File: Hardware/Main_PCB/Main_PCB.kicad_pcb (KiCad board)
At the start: 2 copper layers, 80 x 35 mm, 86 parts, among them J201 Sonar, J601 Conn_01x08_Pin, J602 Conn_01x03_Pin, J603 Servo con, P301 USB_C_Plug_USB2.0, SW301 TL3342F160QG_TR, SW302 TL3342F160QG_TR, U201 TUSS4470TRTJT, U301 RP2040, U302 W25Q128JVS, U401 TPS62170DSG, U402 TPS61175PWPR, U403 BD50FD0WFP2-E2, U501 ICM-42688-P, U601 NRF24L01, U602 SN74LV1T34DBV, Y301 12Mhz

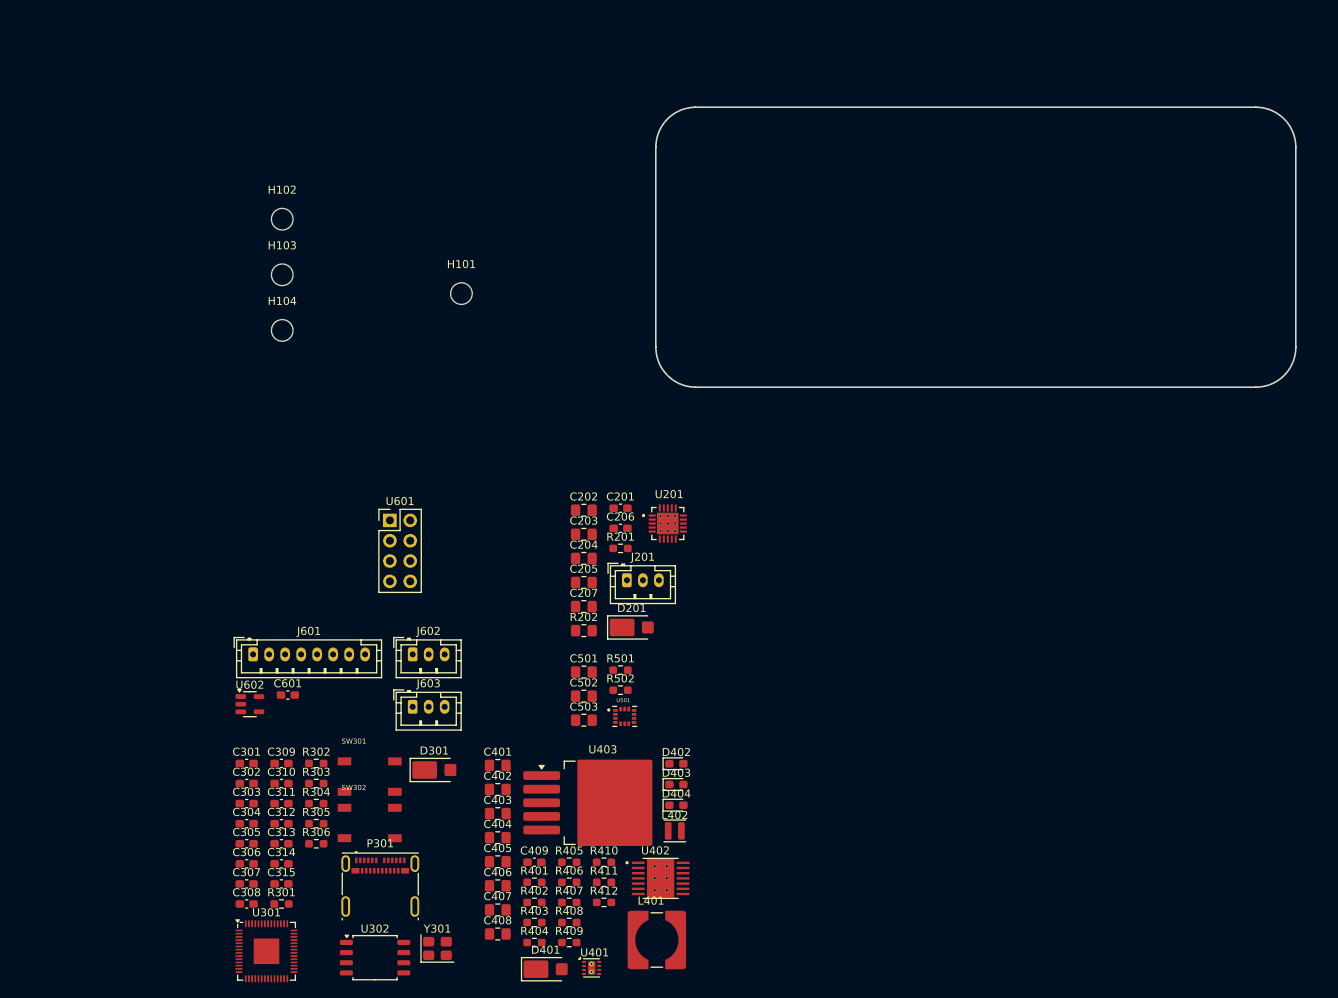
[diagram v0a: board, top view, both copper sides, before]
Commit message: Some footprint positioning
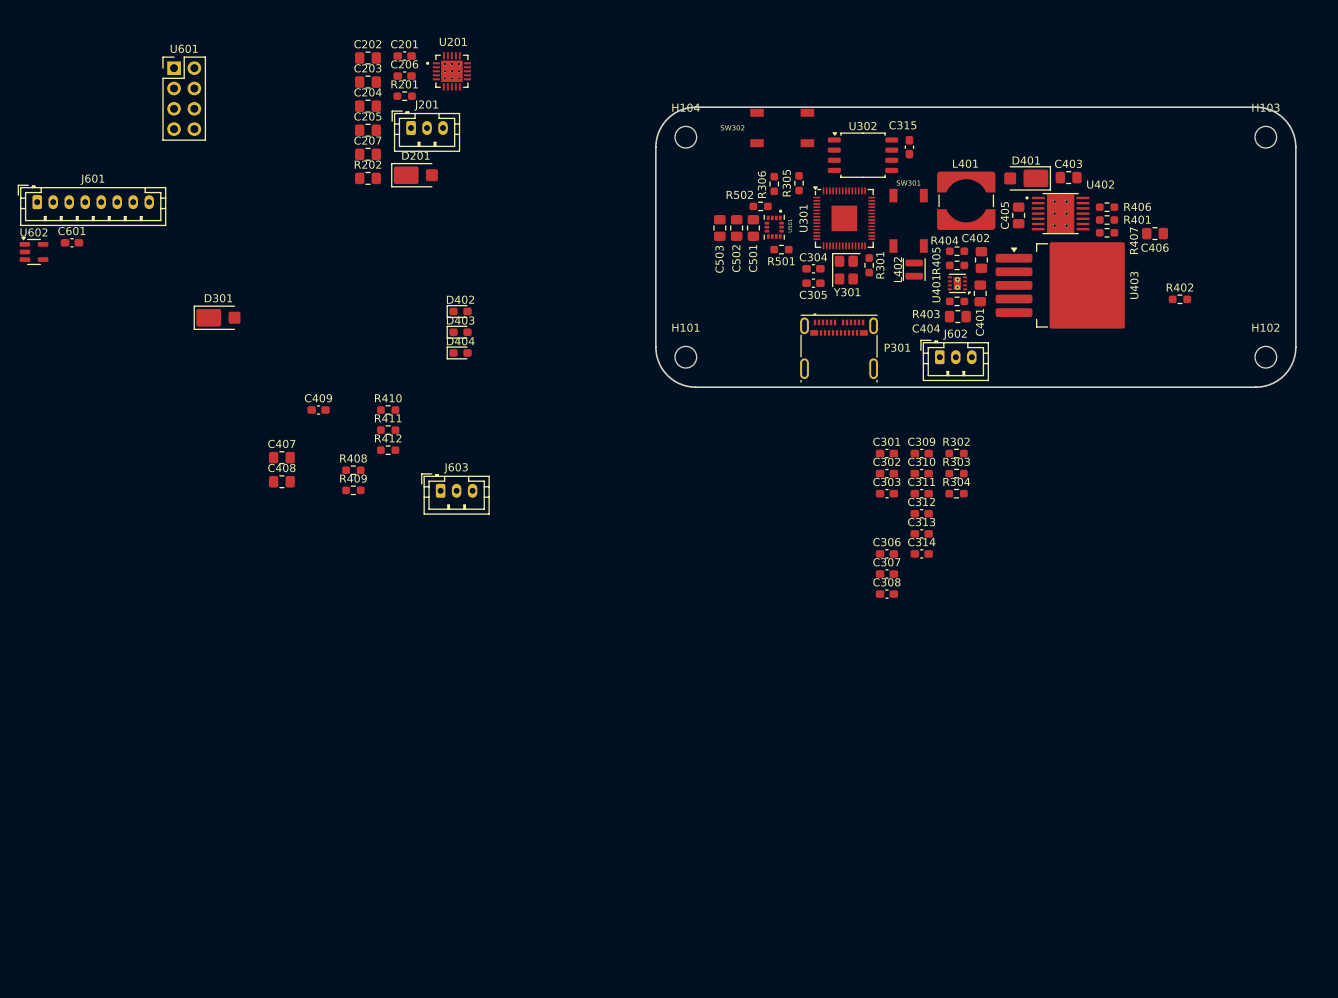
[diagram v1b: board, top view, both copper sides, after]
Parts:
- moved H102 124.2 mm to (191.5, 96.2)
- moved H103 124.1 mm to (191.5, 68.7)
- moved C315 121.0 mm to (146.9, 69.9), turned to -90 degrees
- moved U302 117.4 mm to (141.1, 70.9)
- moved U301 116.7 mm to (138.8, 78.8)
- moved C406 115.7 mm to (177.6, 80.7)
- moved D401 115.7 mm to (161.5, 73.8), turned to 180 degrees
- moved R402 110.4 mm to (180.7, 88.9)
- moved R401 109.4 mm to (171.6, 79.0), turned to 180 degrees
- moved R301 108.5 mm to (141.9, 84.7), turned to -90 degrees
- moved R406 107.9 mm to (171.6, 77.4)
- moved R407 107.4 mm to (171.6, 80.6)
- moved C403 106.8 mm to (166.8, 73.7)
- moved C405 103.8 mm to (160.6, 78.4), turned to 90 degrees
- moved R404 101.3 mm to (152.8, 82.9)
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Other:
- copper layers 2 -> 4

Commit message: Placement almost complete on MainPCB
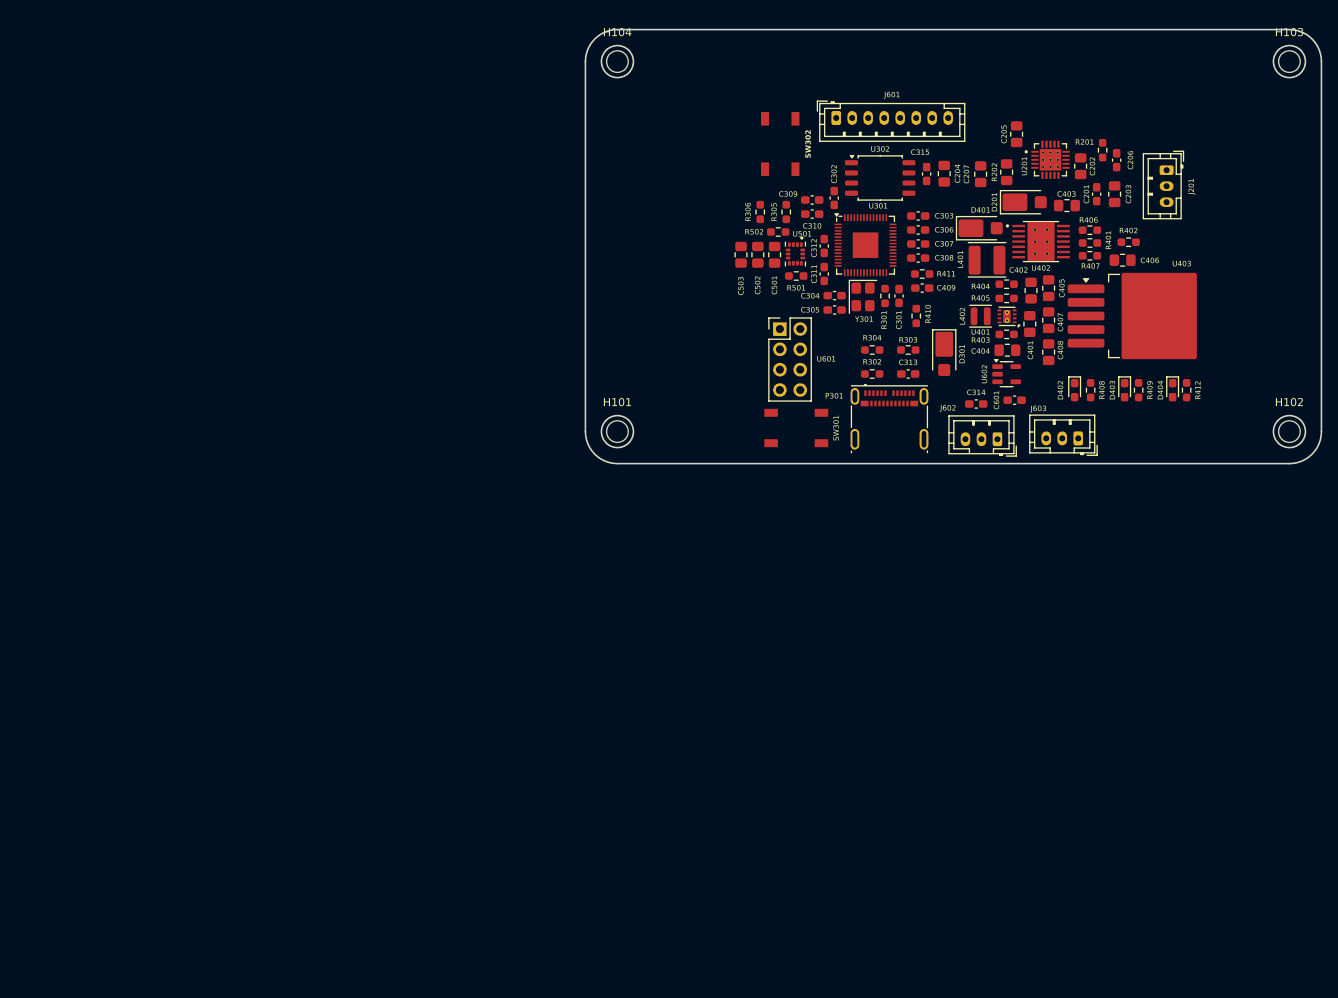
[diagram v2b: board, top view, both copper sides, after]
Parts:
- L401: footprint MainPCB:IND_SRR6038-100Y -> MainPCB:L_33uH
- moved U602 122.5 mm to (159.1, 98.3)
- moved C601 119.5 mm to (160.1, 101.5), turned to 180 degrees
- moved J601 100.4 mm to (137.8, 66.2)
- moved R412 100.1 mm to (181.6, 100.3), turned to -90 degrees
- moved R409 99.0 mm to (175.6, 100.3), turned to -90 degrees
- moved C407 97.4 mm to (164.3, 91.5), turned to -90 degrees
- moved C408 97.2 mm to (164.3, 95.5), turned to -90 degrees
- moved J201 94.6 mm to (179.1, 72.8), turned to -90 degrees
- moved C203 94.4 mm to (172.6, 75.8), turned to 90 degrees
- moved R408 92.7 mm to (169.6, 100.3), turned to -90 degrees
- moved D301 90.8 mm to (151.2, 95.8), turned to -90 degrees
- moved C202 90.1 mm to (168.3, 72.3), turned to 90 degrees
- moved C206 89.6 mm to (172.8, 71.5), turned to -90 degrees
- moved D404 89.1 mm to (179.8, 100.3), turned to -90 degrees
- moved C201 88.2 mm to (170.3, 75.8), turned to 90 degrees
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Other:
- board size 80 x 35 mm -> 92 x 54.2 mm

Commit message: Probably a final version of the MAIN PCB component placement
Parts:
- P301: footprint Connector_USB:USB_C_Receptacle_Molex_105450-0101 -> MainPCB:CUI_UJC-HP-3-SMT-TR
- U601: footprint Connector_PinHeader_2.54mm:PinHeader_2x04_P2.54mm_Vertical -> Connector_PinSocket_2.54mm:PinSocket_2x04_P2.54mm_Vertical
- moved H104 27.5 mm to (137.4, 64.5)
- moved H101 27.0 mm to (137.4, 105.5)
- moved R502 15.3 mm to (145.7, 78.7)
- moved SW301 14.8 mm to (147.6, 105.0)
- moved D402 14.7 mm to (182.2, 98.3)
- moved D403 14.7 mm to (188.4, 98.3)
- moved D404 14.7 mm to (194.4, 98.3)
- moved R408 14.7 mm to (184.2, 98.3)
- moved R409 14.7 mm to (190.2, 98.3)
- moved R412 14.7 mm to (196.2, 98.3)
- moved U501 14.7 mm to (147.2, 81.6)
- moved U403 14.6 mm to (191.2, 90.2)
- moved P301 14.6 mm to (159.0, 102.5)
- moved R305 14.6 mm to (146.0, 76.2)
- moved R306 14.6 mm to (142.7, 76.2)
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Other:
- board outline removed

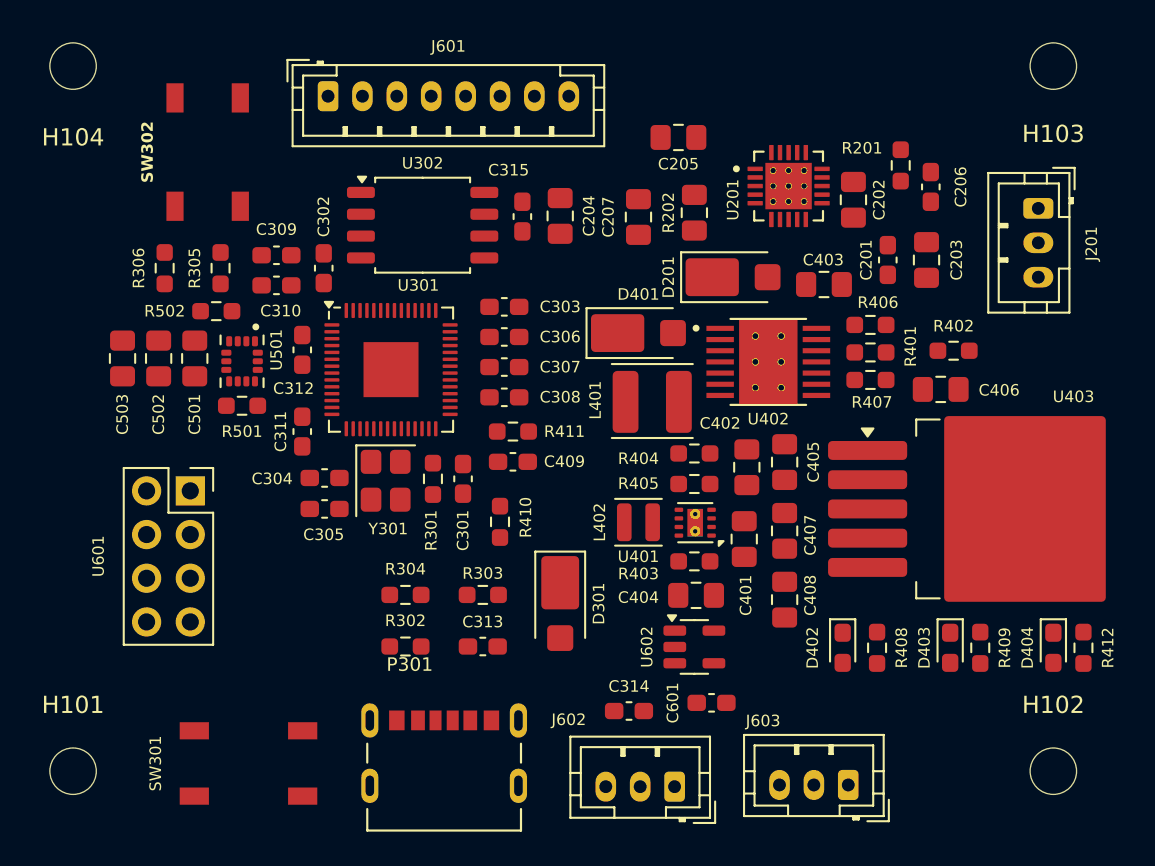
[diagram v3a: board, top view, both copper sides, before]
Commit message: Made the power supply planes and traces
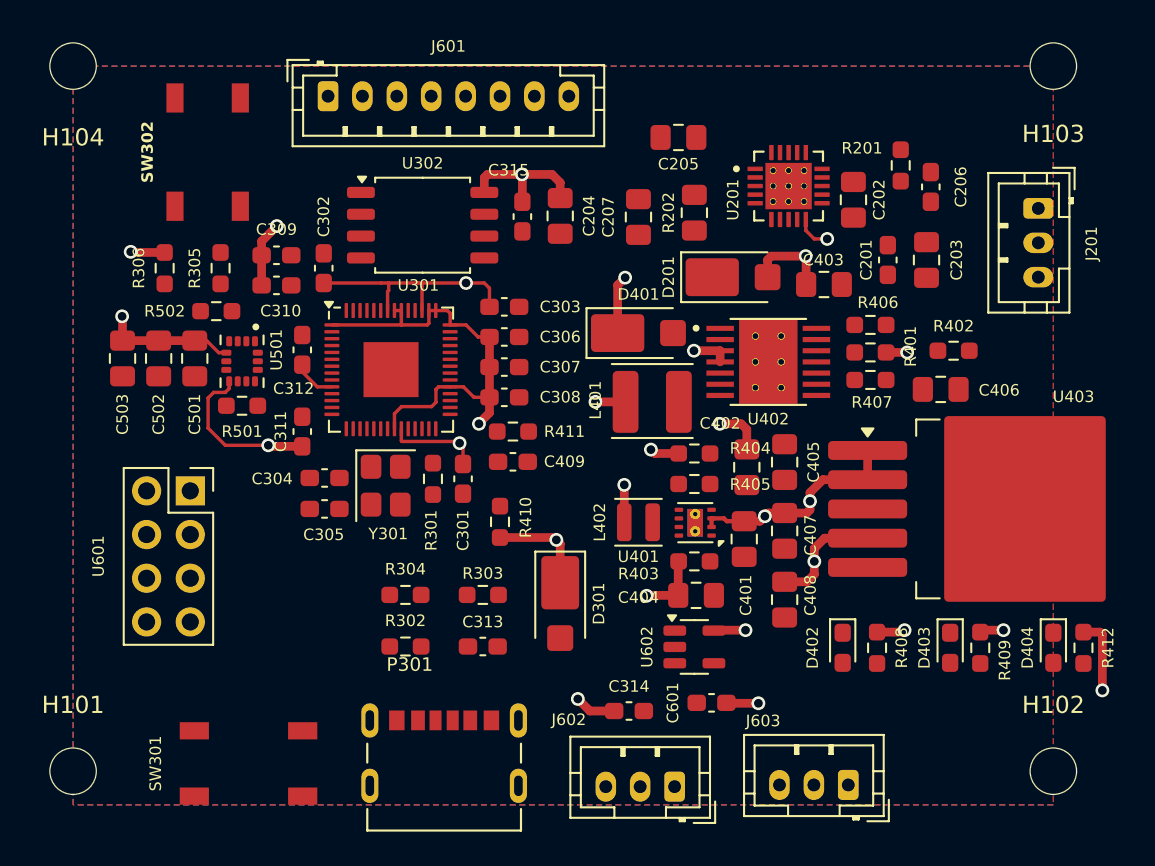
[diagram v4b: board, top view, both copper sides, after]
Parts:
- moved Y301 0.29 mm to (155.6, 88.8)
- turned R404 to 180 degrees
- turned R405 to 0 degrees
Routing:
- net +3.3V: track 0.00 -> 72.8 mm, vias 0 -> 12
- net +1V1: track 0.00 -> 29.2 mm, vias 0 -> 2
- net VDC: track 0.00 -> 25.7 mm, vias 0 -> 6
- net +12V: track 0.00 -> 14.0 mm, vias 0 -> 4
- net +5V: track 0.00 -> 12.0 mm, vias 0 -> 4
- added copper zone on In2.Cu, net +12V
- added copper zone on In2.Cu, net +3.3V
- added copper zone on In2.Cu, net +5V
- added copper zone on B.Cu, net GND
- added copper zone on F.Cu, net GND
- added copper zone on In1.Cu, net GND
- added copper zone on In2.Cu, net VDC

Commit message: Work on the PCB
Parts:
- moved C403 79.6 mm to (101.8, 70.0)
- moved C404 72.7 mm to (101.5, 86.5)
- moved L402 72.3 mm to (98.2, 84.5), turned to -90 degrees
- moved C314 72.2 mm to (98.0, 93.8)
- moved J603 72.2 mm to (110.7, 98.5)
- moved R403 72.2 mm to (101.5, 88.5)
- moved C201 72.1 mm to (113.0, 68.8)
- moved C203 72.1 mm to (115.2, 68.8)
- moved C206 72.1 mm to (115.5, 64.5)
- moved C207 72.1 mm to (98.5, 66.3)
- moved C304 72.1 mm to (80.2, 81.5)
- moved C305 72.1 mm to (80.2, 83.2)
- moved C315 72.1 mm to (91.8, 66.2)
- moved C401 72.1 mm to (104.7, 85.0)
- moved C405 72.1 mm to (107.0, 80.5)
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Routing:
- net GND: track 0.00 -> 31.0 mm, vias 0 -> 9
- net +3.3V: track 72.8 -> 80.7 mm, vias 12 -> 11
- net VDC: track 25.7 -> 23.6 mm
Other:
- board outline added: 65 x 49 mm

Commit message: Finished the routing - V1
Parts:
- moved R303 4.54 mm to (84.9, 88.5), turned to 0 degrees
- moved R304 4.47 mm to (89.4, 88.5), turned to 180 degrees
- moved R407 1.38 mm to (112.7, 77.0)
- moved C311 0.97 mm to (78.1, 79.2)
- moved R401 0.80 mm to (112.8, 74.3)
- moved R402 0.76 mm to (117.6, 74.2)
- moved C312 0.73 mm to (78.4, 73.5)
- moved C406 0.71 mm to (116.8, 76.5)
- moved C313 0.49 mm to (89.0, 91.3)
- moved C304 0.35 mm to (80.2, 81.8)
- moved C301 0.15 mm to (88.3, 81.7)
- moved C302 0.15 mm to (80.2, 69.4)
- moved C303 0.15 mm to (90.7, 71.7)
- moved C305 0.15 mm to (80.2, 83.4)
- moved C306 0.15 mm to (90.7, 73.4)
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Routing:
- net /OUT3: track 0.00 -> 124.1 mm, vias 0 -> 4
- net /OUT4: track 0.00 -> 112.6 mm, vias 0 -> 4
- net /RP2040/GPIO5: track 0.00 -> 91.1 mm, vias 0 -> 2
- net /RP2040/GPIO4: track 0.00 -> 71.7 mm, vias 0 -> 2
- net /RP2040/GPIO2: track 0.00 -> 61.0 mm, vias 0 -> 2
- net /RP2040/GPIO3: track 0.00 -> 59.7 mm, vias 0 -> 4
- net /RP2040/GPIO1: track 0.00 -> 57.2 mm, vias 0 -> 2
- net /RP2040/GPIO0: track 0.00 -> 53.6 mm, vias 0 -> 2
- net /ALS: track 0.00 -> 51.0 mm, vias 0 -> 1
- net /AHS: track 0.00 -> 49.8 mm, vias 0 -> 1
- net /BHS: track 0.00 -> 48.8 mm, vias 0 -> 1
- net Net-(U201-VDRV): track 0.00 -> 45.9 mm
- net /BEMF: track 0.00 -> 45.5 mm, vias 0 -> 1
- net /CLS: track 0.00 -> 45.2 mm, vias 0 -> 2
- net /CHS: track 0.00 -> 43.3 mm, vias 0 -> 1
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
